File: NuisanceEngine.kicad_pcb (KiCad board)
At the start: 2 copper layers, 58 x 53 mm, 59 parts, among them J1 CV, J2 Headphones, J3 Power, Q1 2N3904, Q2 2N3904, Q3 TIP31A, Q4 TIP32A, SW1 SW_SPDT, SW2 SW_SPDT, U1 LM324

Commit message: finished new layout, gonna double check tomorrow morning
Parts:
- D1: moved to B.Cu
- moved R1 41.3 mm to (54.0, 66.2)
- moved LOGO 19.1 mm to (64.5, 47.5)
- moved Q3 15.4 mm to (74.0, 50.5), turned to 270 degrees
- moved Q1 12.1 mm to (62.5, 67.0)
- moved R25 11.7 mm to (74.8, 59.0), turned to 90 degrees
- moved R4 10.5 mm to (56.5, 66.2)
- moved R8 10.5 mm to (63.2, 71.0), turned to 0 degrees
- moved C9 8.95 mm to (65.8, 61.8)
- moved R20 8.87 mm to (73.8, 66.2)
- moved R21 8.55 mm to (73.8, 68.2)
- moved C4 8.19 mm to (63.2, 74.0), turned to 0 degrees
- moved R2 7.72 mm to (59.0, 66.2), turned to 270 degrees
- moved D1 6.18 mm to (75.5, 63.5), turned to 0 degrees
- moved R24 6.15 mm to (71.8, 59.0)
- moved Q4 5.22 mm to (68.5, 50.5), turned to 270 degrees
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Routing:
- net Net-(J1-Pad2): track 7.96 -> 46.3 mm, vias 0 -> 1
- net Net-(R1-Pad2): track 43.0 -> 16.0 mm, vias 2 -> 0
- net Net-(C8-Pad1): track 33.2 -> 11.1 mm
- net VDD: track 61.7 -> 83.2 mm
- net Net-(R20-Pad2): track 14.7 -> 4.30 mm, vias 2 -> 0
- net GND: track 1.00 -> 8.18 mm, vias 26 -> 25
- net Net-(R14-Pad2): track 31.9 -> 25.2 mm
- net Net-(Q1-Pad1): track 5.85 -> 10.7 mm
- net Net-(C4-Pad1): track 14.2 -> 18.9 mm
- net Net-(R2-Pad1): track 7.35 -> 2.98 mm
- net Net-(C8-Pad2): track 27.3 -> 23.1 mm
- net Net-(C7-Pad1): track 21.2 -> 18.5 mm
- net Net-(R12-Pad1): track 7.12 -> 5.23 mm
- net Net-(D2-Pad2): track 6.24 -> 4.49 mm
- net Net-(J3-Pad2): track 41.2 -> 42.6 mm
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
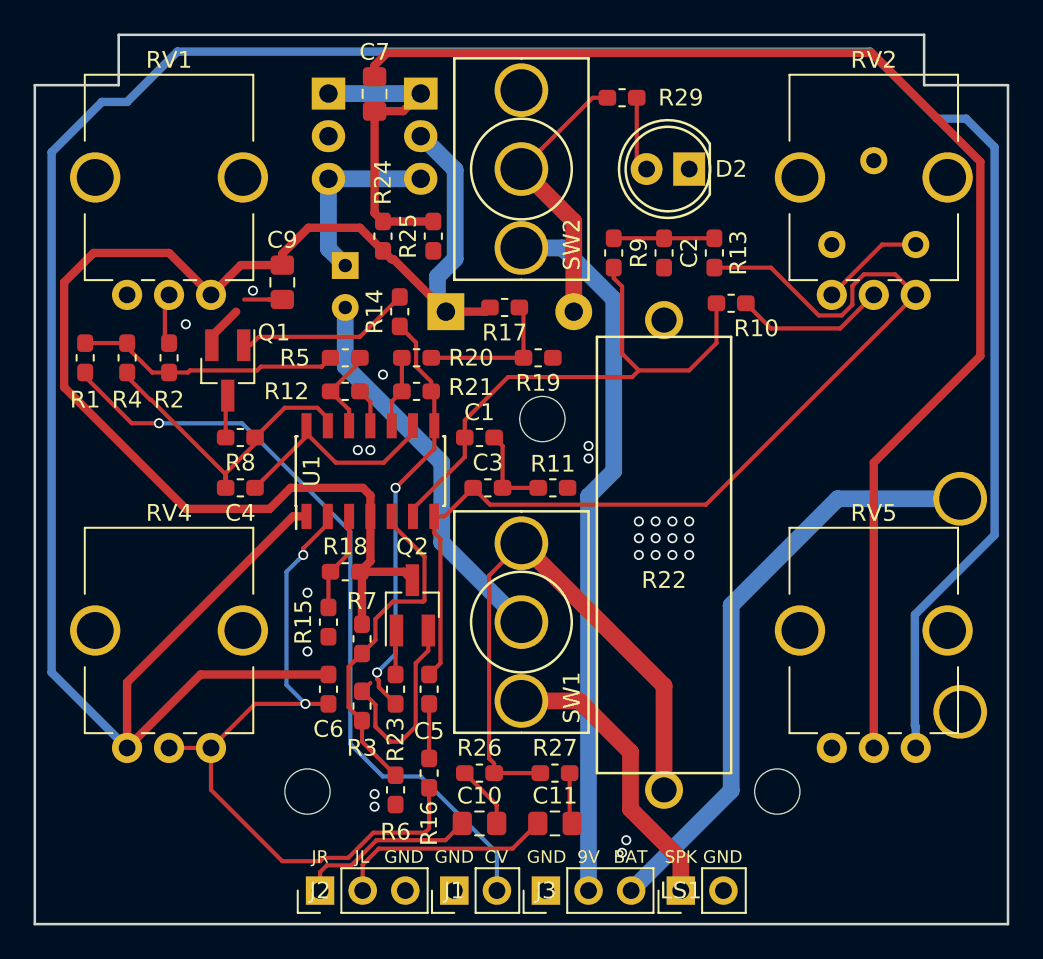
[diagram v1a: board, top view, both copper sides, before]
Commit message: moved trimpot from under potentiometer
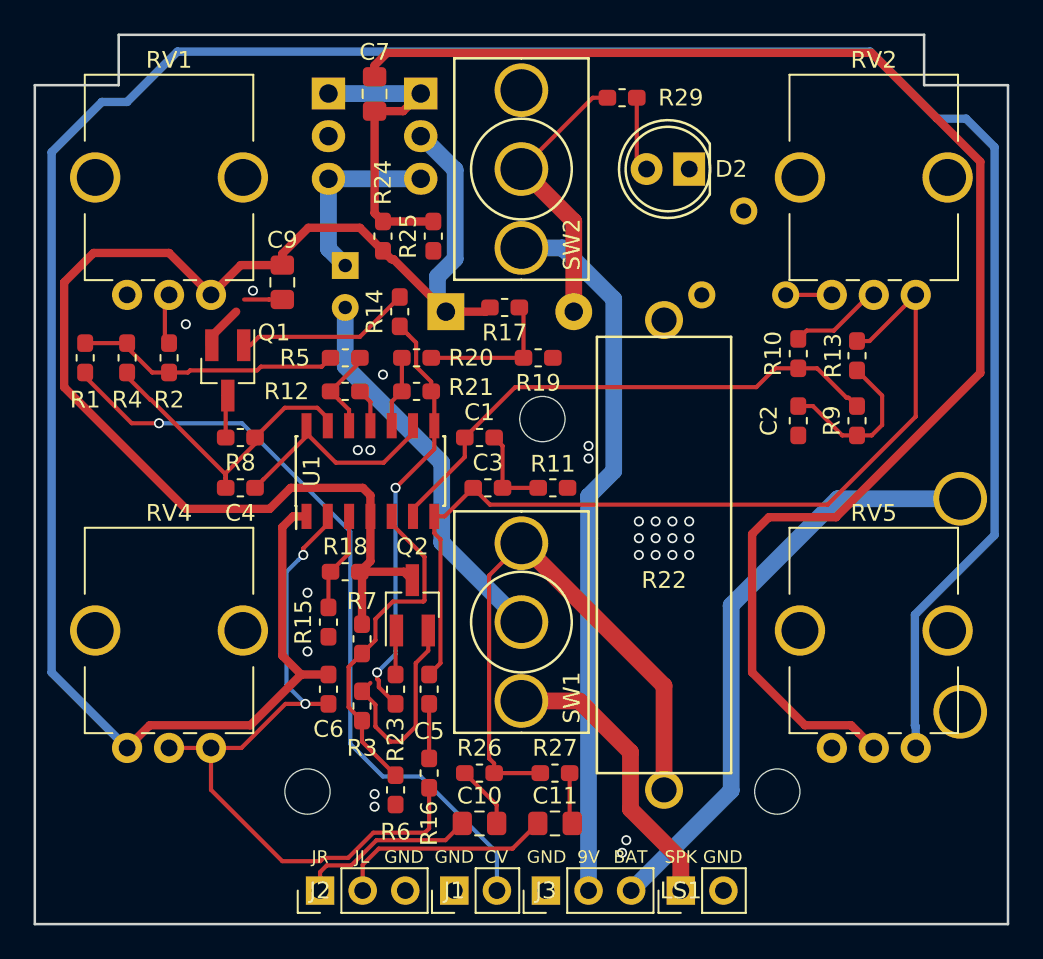
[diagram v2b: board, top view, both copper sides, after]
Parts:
- moved R9 17.6 mm to (100.0, 70.0), turned to 270 degrees
- moved C2 12.8 mm to (96.5, 70.0)
- moved R13 10.5 mm to (100.0, 66.1), turned to 90 degrees
- moved RV3 8.31 mm to (90.8, 62.5)
- moved R10 5.00 mm to (96.5, 66.0), turned to 90 degrees
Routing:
- net Net-(C7-Pad2): track 77.3 -> 87.3 mm
- net Net-(C6-Pad1): track 168.7 -> 161.0 mm
- net Net-(C3-Pad1): track 60.2 -> 53.7 mm
- net Net-(C2-Pad2): track 6.00 -> 9.86 mm
- net Net-(RV2-Pad1): track 6.24 -> 2.75 mm
- net Net-(R10-Pad2): track 9.07 -> 5.59 mm
- net Net-(C1-Pad2): track 33.0 -> 32.0 mm
